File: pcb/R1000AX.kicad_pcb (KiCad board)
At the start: 4 copper layers, 175 x 65.5 mm, 140 parts, among them J1 PCIESOCKET-X1, J10 PCIESOCKET-X1, J11 PCIESOCKET-X1, J12 PCIESOCKET-X1, J13 PCIESOCKET-X1, J14 PCIESOCKET-X1, J15 PCIESOCKET-X1, J16 CONN127P-02X05, J17 USB_B_RECEPTACLE, J18 SOCKET254P-01X02, J19 COMPUTE_MOD_1, J2 PCIESOCKET-X1, J20 USB_A_RECEPTACLE_2, J25 SOCKET420P-02X04-CPU, J3 PCIESOCKET-X1, J31 USB_A_RECEPTACLE_2, J4 PCIESOCKET-X1, J5 PCIESOCKET-X1, J6 PCIESOCKET-X1, J7 PCIESOCKET-X1, J8 PCIESOCKET-X1, J81 SOCKET254P-01X02, J82 SOCKET254P-01X02, J83 SOCKET254P-01X02, J9 PCIESOCKET-X1, Q1 DMG2305UX-7, Q2 PSMN1R2-30YLC, Q3 Q_PNP_BEC, Q4 Q_NPN_BEC, Q5 Q_PNP_BEC, Q6 Q_PNP_BEC, U1 LPC1769FBD100,551, U2 AP3418, U20 M24C08-FDW6TP, U3 BD9E302EFJ-E2, U4 INA3221AIRGVR, U5 LM5060MM/NOPB, Y1 XTAL4_12MHz

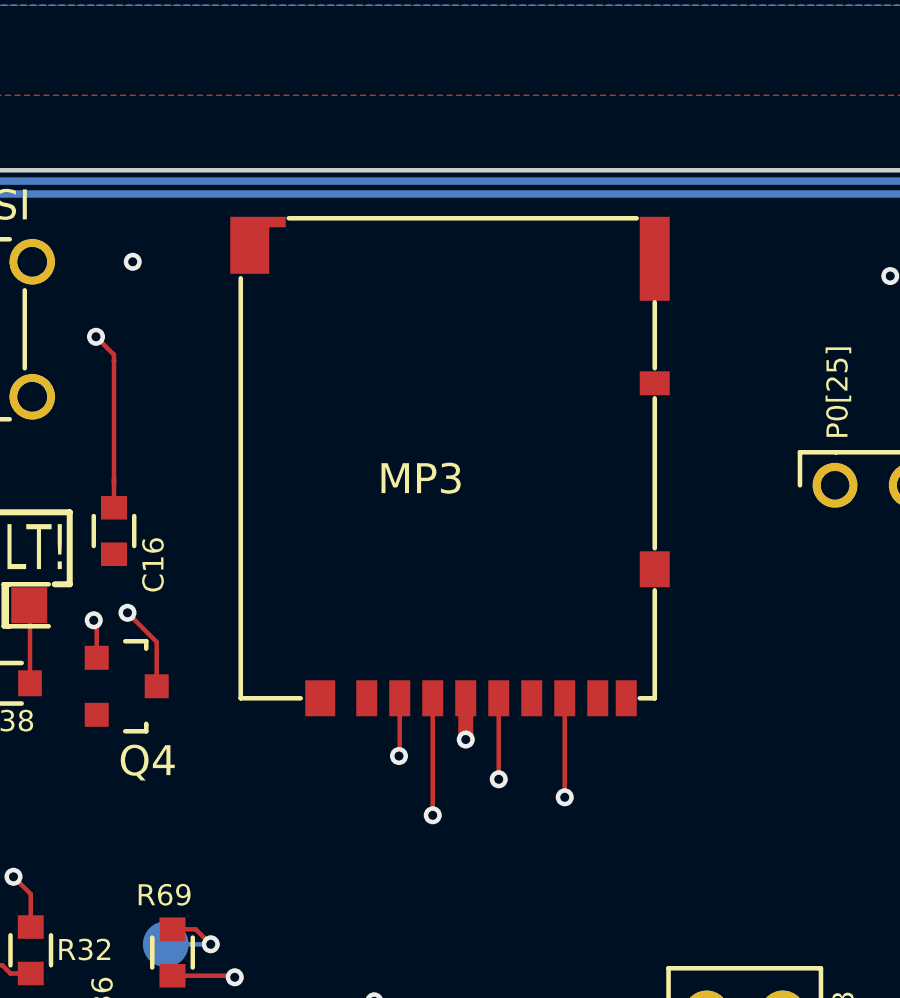
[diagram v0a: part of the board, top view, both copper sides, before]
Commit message: moved SD card more towards edge, making it accessible from case
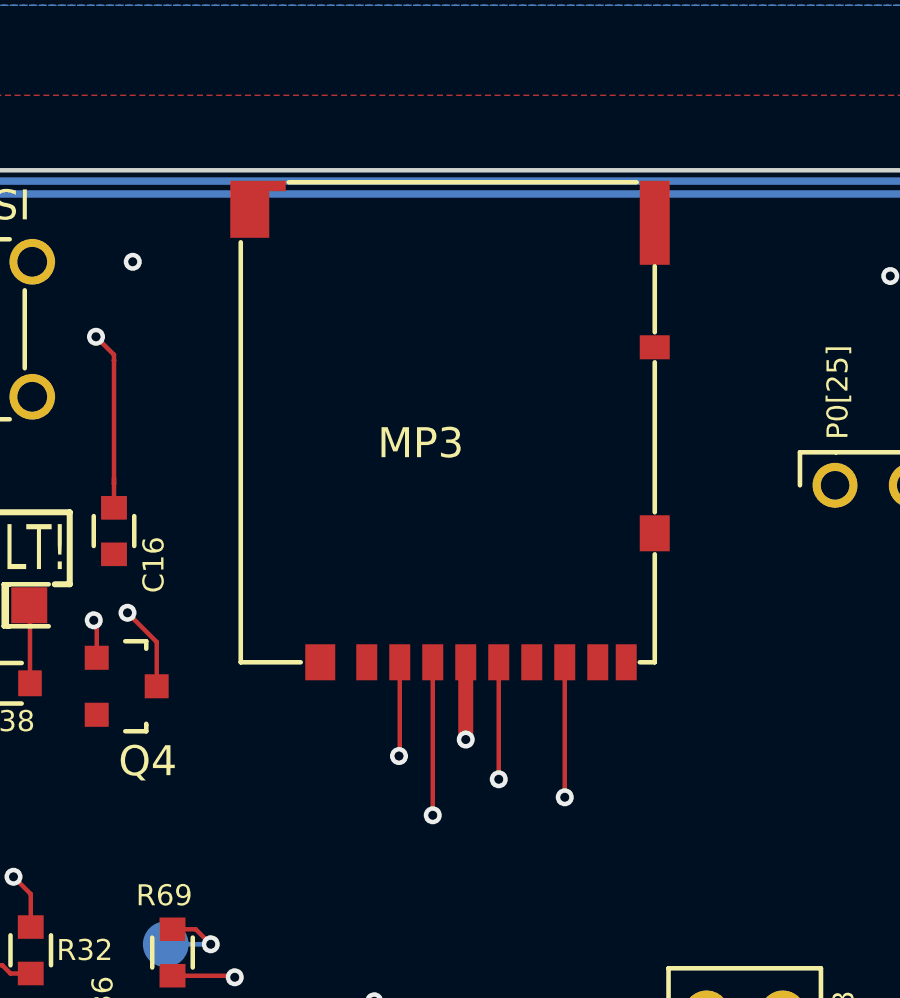
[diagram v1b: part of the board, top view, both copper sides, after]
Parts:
- moved MP3 1.20 mm to (165.8, 89.3)
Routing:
- net +3V3: track 53.4 -> 54.6 mm
- net SD_SSEL: track 52.2 -> 53.4 mm
- net SD_SCK: track 55.0 -> 56.2 mm
- net SD_MOSI: track 52.3 -> 53.5 mm
- net SD_MISO: track 56.8 -> 58.0 mm
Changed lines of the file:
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@@
     (thickness 1.6)
     (drawings 72)
-    (tracks 3447)
+    (tracks 3448)
     (zones 0)
     (modules 140)
@@
   (page A4)
   (layers
-    (0 F.Cu signal hide)
+    (0 F.Cu signal)
     (1 In1.Cu signal hide)
     (2 In2.Cu signal hide)
@@
     (pad_to_mask_clearance 0)
     (aux_axis_origin -41.6 -108.1)
-    (visible_elements 7FFEFFFF)
+    (visible_elements 7FFE7FFF)
     (pcbplotparams
       (layerselection 0x010fe_80000007)
@@
   )
   (module Main:MICROSD_RECEPTACLE_2 (layer F.Cu)
-    (at 165.8 90.5 180)
+    (at 165.8 89.3 180)
     (fp_text reference MP3 (at -1.8 6.7 180) (layer F.SilkS)
       (effects (font (size 1 1) (thickness 0.15)))
@@
   (gr_arc (start 53 137) (end 53 139) (angle 90) (layer Edge.Cuts) (width 0.15))
   (gr_line (start 51 75.5) (end 51 137) (angle 90) (layer Edge.Cuts) (width 0.15))
+  (segment (start 169.1 92.475) (end 169.1 89.9) (width 0.5) (layer F.Cu) (net 1))
+  (via (at 169.1 92.475) (size 0.6) (drill 0.3) (layers F.Cu B.Cu) (net 1))
   (segment (start 77.40076 77.55) (end 76.05 77.55) (width 0.2) (layer F.Cu) (net 1))
   (via (at 75.8 77.3) (size 0.6) (drill 0.3) (layers F.Cu B.Cu) (net 1))
   (segment (start 76.05 77.55) (end 75.8 77.3) (width 0.2) (layer F.Cu) (net 1))
-  (segment (start 169.1 91.1) (end 169.1 92.475) (width 0.5) (layer F.Cu) (net 1))
-  (via (at 169.1 92.475) (size 0.6) (drill 0.3) (layers F.Cu B.Cu) (net 1))
   (segment (start 131.7 81.2995) (end 132.6495 81.2995) (width 0.25) (layer F.Cu) (net 1))
   (via (at 132.825 81.475) (size 0.6) (drill 0.3) (layers F.Cu B.Cu) (net 1))
@@
   (segment (start 69.14 83.575) (end 66.575 83.575) (width 0.75) (layer F.Cu) (net 90))
   (segment (start 66.575 83.575) (end 66 83) (width 0.75) (layer F.Cu) (net 90))
+  (segment (start 166.9 93) (end 166.9 89.9) (width 0.15) (layer F.Cu) (net 91))
   (segment (start 161.925 93.524994) (end 166.375006 93.524994) (width 0.15) (layer In2.Cu) (net 91))
-  (segment (start 166.9 93) (end 166.9 91.1) (width 0.15) (layer F.Cu) (net 91))
   (segment (start 166.875 93.025) (end 166.9 93) (width 0.15) (layer F.Cu) (net 91))
+  (segment (start 166.9 93) (end 166.9 93) (width 0.15) (layer F.Cu) (net 91))
   (via (at 166.875 93.025) (size 0.6) (drill 0.3) (layers F.Cu B.Cu) (net 91))
   (segment (start 166.375006 93.524994) (end 166.875 93.025) (width 0.15) (layer In2.Cu) (net 91))
@@
   (segment (start 161.925736 93.524994) (end 161.925 93.524994) (width 0.15) (layer In2.Cu) (net 91))
   (segment (start 161.925 93.524994) (end 150.672792 93.524994) (width 0.15) (layer In2.Cu) (net 91))
-  (segment (start 168 95) (end 168 94.7) (width 0.15) (layer In2.Cu) (net 92))
-  (via (at 168 95) (size 0.6) (drill 0.3) (layers F.Cu B.Cu) (net 92))
-  (segment (start 168 91.1) (end 168 95) (width 0.15) (layer F.Cu) (net 92))
-  (segment (start 168 94.7) (end 167.725 94.425) (width 0.15) (layer In2.Cu) (net 92))
-  (segment (start 167.725 94.425) (end 150.3 94.425) (width 0.15) (layer In2.Cu) (net 92))
-  (segment (start 126.710281 86.775) (end 124.687363 88.797918) (width 0.15) (layer F.Cu) (net 92))
-  (segment (start 126.9 86.775) (end 126.710281 86.775) (width 0.15) (layer F.Cu) (net 92))
-  (via (at 126.9 86.775) (size 0.6) (drill 0.3) (layers F.Cu B.Cu) (net 92))
-  (segment (start 126.633463 87.041537) (end 126.9 86.775) (width 0.15) (layer In2.Cu) (net 92))
-  (segment (start 126.633463 87.316537) (end 126.633463 87.041537) (width 0.15) (layer In2.Cu) (net 92))
-  (segment (start 133.066926 93.75) (end 126.633463 87.316537) (width 0.15) (layer In2.Cu) (net 92))
-  (segment (start 149.625 93.75) (end 133.066926 93.75) (width 0.15) (layer In2.Cu) (net 92))
+  (segment (start 168 89.9) (end 168 95) (width 0.15) (layer F.Cu) (net 92))
   (segment (start 150.3 94.425) (end 149.625 93.75) (width 0.15) (layer In2.Cu) (net 92))
-  (segment (start 162 93.824996) (end 170.175004 93.824996) (width 0.15) (layer In2.Cu) (net 93))
-  (via (at 170.2 93.8) (size 0.6) (drill 0.3) (layers F.Cu B.Cu) (net 93))
-  (segment (start 170.2 93.8) (end 170.2 91.1) (width 0.15) (layer F.Cu) (net 93))
+  (segment (start 149.625 93.75) (end 133.066926 93.75) (width 0.15) (layer In2.Cu) (net 92))
+  (segment (start 133.066926 93.75) (end 126.633463 87.316537) (width 0.15) (layer In2.Cu) (net 92))
+  (segment (start 126.633463 87.316537) (end 126.633463 87.041537) (width 0.15) (layer In2.Cu) (net 92))
+  (segment (start 126.633463 87.041537) (end 126.9 86.775) (width 0.15) (layer In2.Cu) (net 92))
+  (via (at 126.9 86.775) (size 0.6) (drill 0.3) (layers F.Cu B.Cu) (net 92))
+  (segment (start 126.9 86.775) (end 126.710281 86.775) (width 0.15) (layer F.Cu) (net 92))
+  (segment (start 126.710281 86.775) (end 124.687363 88.797918) (width 0.15) (layer F.Cu) (net 92))
+  (segment (start 167.725 94.425) (end 150.3 94.425) (width 0.15) (layer In2.Cu) (net 92))
+  (segment (start 168 94.7) (end 167.725 94.425) (width 0.15) (layer In2.Cu) (net 92))
+  (via (at 168 95) (size 0.6) (drill 0.3) (layers F.Cu B.Cu) (net 92))
+  (segment (start 168 95) (end 168 94.7) (width 0.15) (layer In2.Cu) (net 92))
+  (segment (start 170.2 89.9) (end 170.2 93.8) (width 0.15) (layer F.Cu) (net 93))
   (segment (start 170.175004 93.824996) (end 170.2 93.8) (width 0.15) (layer In2.Cu) (net 93))
+  (via (at 170.2 93.8) (size 0.6) (drill 0.3) (layers F.Cu B.Cu) (net 93))
+  (segment (start 170.175004 93.824996) (end 162 93.824996) (width 0.15) (layer In2.Cu) (net 93))
   (segment (start 127.05 85) (end 123.980256 88.069744) (width 0.15) (layer F.Cu) (net 93))
   (via (at 127.05 85) (size 0.6) (drill 0.3) (layers F.Cu B.Cu) (net 93))
@@
   (segment (start 162 93.824996) (end 150.548528 93.824996) (width 0.15) (layer In2.Cu) (net 93))
   (segment (start 123.980256 88.069744) (end 123.980256 88.090812) (width 0.15) (layer F.Cu) (net 93))
-  (segment (start 163.175 94.124998) (end 169.424998 94.124998) (width 0.15) (layer In2.Cu) (net 94))
-  (via (at 172.4 94.4) (size 0.6) (drill 0.3) (layers F.Cu B.Cu) (net 94))
-  (segment (start 172.4 94.4) (end 172.4 91.1) (width 0.15) (layer F.Cu) (net 94))
-  (segment (start 169.7 94.4) (end 172.4 94.4) (width 0.15) (layer In2.Cu) (net 94))
+  (segment (start 172.4 89.9) (end 172.4 94.4) (width 0.15) (layer F.Cu) (net 94))
   (segment (start 169.424998 94.124998) (end 169.7 94.4) (width 0.15) (layer In2.Cu) (net 94))
+  (segment (start 169.7 94.4) (end 172.4 94.4) (width 0.15) (layer In2.Cu) (net 94))
+  (via (at 172.4 94.4) (size 0.6) (drill 0.3) (layers F.Cu B.Cu) (net 94))
+  (segment (start 169.424998 94.124998) (end 163.175 94.124998) (width 0.15) (layer In2.Cu) (net 94))
   (segment (start 126.878175 85.9) (end 124.33381 88.444365) (width 0.15) (layer F.Cu) (net 94))
   (segment (start 127.075 85.9) (end 126.878175 85.9) (width 0.15) (layer F.Cu) (net 94))

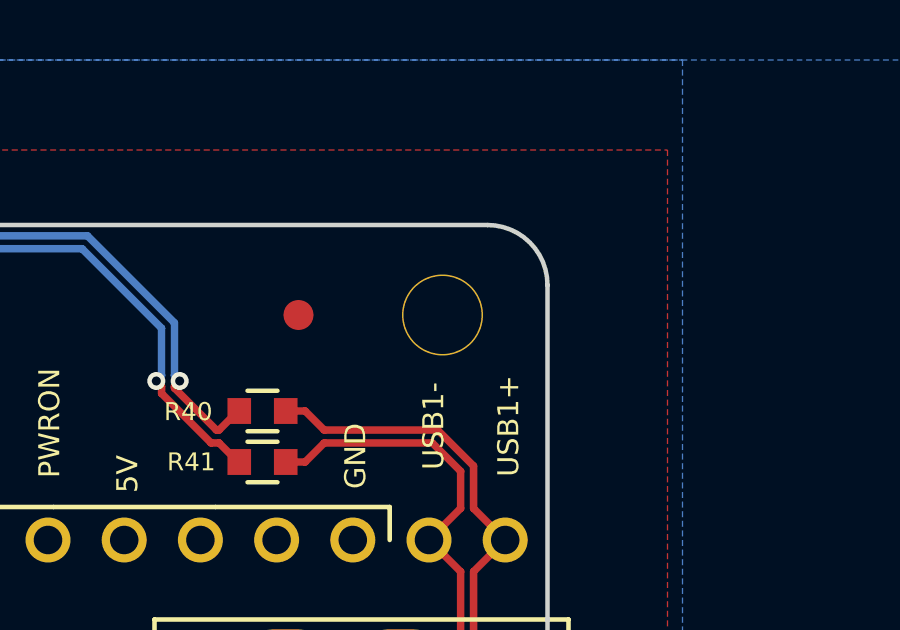
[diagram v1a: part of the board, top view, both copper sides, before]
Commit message: re-exported gerbers, moved SD card towards edge
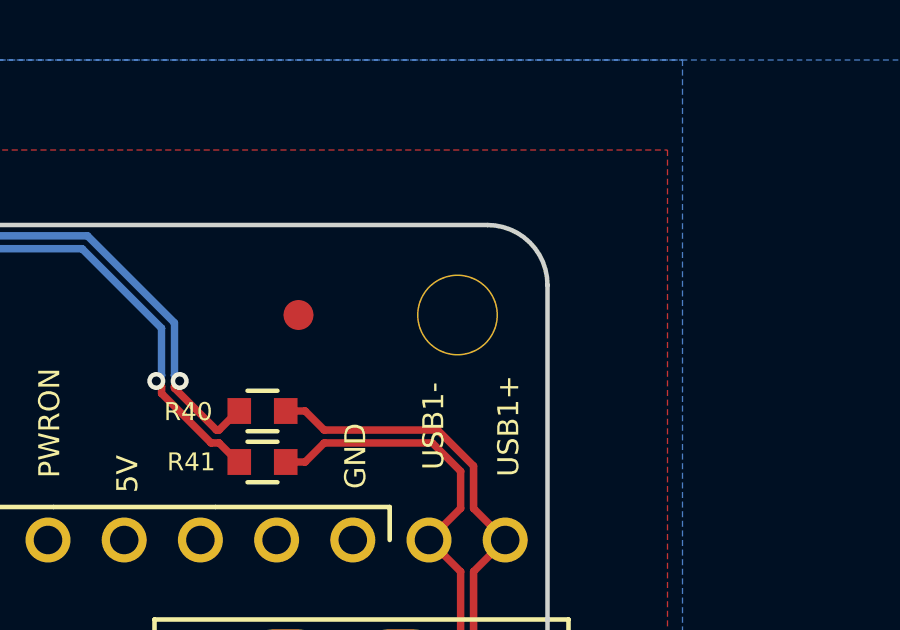
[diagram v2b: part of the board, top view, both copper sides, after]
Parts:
- moved MP8 9.38 mm to (223.0, 76.5)
- moved MP7 6.40 mm to (54.0, 136.0)
- moved MP4 1.41 mm to (223.0, 136.0)
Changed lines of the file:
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@@
     )
-  )
-  (module Main:MECH_NPTH_M3 (layer F.Cu)
-    (at 222 135)
-    (fp_text reference MP4 (at 0 -1.6) (layer F.SilkS) hide
-      (effects (font (size 1 1) (thickness 0.15)))
-    )
-    (fp_text value MECH_NPTH_M3 (at 0 -2.8) (layer F.Fab) hide
-      (effects (font (size 1 1) (thickness 0.15)))
-    )
-    (pad "" np_thru_hole circle (at 1 1) (size 2.7 2.7) (drill 2.6) (layers *.Cu *.Mask F.SilkS))
-  )
-  (module Main:MECH_NPTH_M3 (layer F.Cu)
-    (at 85 76.5)
-    (fp_text reference MP6 (at 0 -1.6) (layer F.SilkS) hide
-      (effects (font (size 1 1) (thickness 0.15)))
-    )
-    (fp_text value MECH_NPTH_M3 (at 0 -2.8) (layer F.Fab) hide
-      (effects (font (size 1 1) (thickness 0.15)))
-    )
-    (pad "" np_thru_hole circle (at 0 0) (size 2.7 2.7) (drill 2.6) (layers *.Cu *.Mask F.SilkS))
-  )
-  (module Main:MECH_NPTH_M3 (layer F.Cu)
-    (at 49 140)
-    (fp_text reference MP7 (at 0 -1.6) (layer F.SilkS) hide
-      (effects (font (size 1 1) (thickness 0.15)))
-    )
-    (fp_text value MECH_NPTH_M3 (at 0 -2.8) (layer F.Fab) hide
-      (effects (font (size 1 1) (thickness 0.15)))
-    )
-    (pad "" np_thru_hole circle (at 5 -4) (size 2.7 2.7) (drill 2.6) (layers *.Cu *.Mask F.SilkS))
-  )
-  (module Main:MECH_NPTH_M3 (layer F.Cu)
-    (at 221.8 85.8)
-    (fp_text reference MP8 (at 0 -1.6) (layer F.SilkS) hide
-      (effects (font (size 1 1) (thickness 0.15)))
-    )
-    (fp_text value MECH_NPTH_M3 (at 0 -2.8) (layer F.Fab) hide
-      (effects (font (size 1 1) (thickness 0.15)))
-    )
-    (pad "" np_thru_hole circle (at 0.7 -9.3) (size 2.7 2.7) (drill 2.6) (layers *.Cu *.Mask F.SilkS))
   )
   (module Main:COMPUTE_MOD_1 (layer F.Cu)
@@
     )
   )
+  (module Main:MECH_NPTH_M3 (layer F.Cu)
+    (at 223 136)
+    (fp_text reference MP4 (at 0 -1.6) (layer F.SilkS) hide
+      (effects (font (size 1 1) (thickness 0.15)))
+    )
+    (fp_text value MECH_NPTH_M3 (at 0 -2.8) (layer F.Fab) hide
+      (effects (font (size 1 1) (thickness 0.15)))
+    )
+    (pad "" np_thru_hole circle (at 0 0) (size 2.7 2.7) (drill 2.6) (layers *.Cu *.Mask F.SilkS))
+  )
+  (module Main:MECH_NPTH_M3 (layer F.Cu)
+    (at 54 136)
+    (fp_text reference MP7 (at 0 -1.6) (layer F.SilkS) hide
+      (effects (font (size 1 1) (thickness 0.15)))
+    )
+    (fp_text value MECH_NPTH_M3 (at 0 -2.8) (layer F.Fab) hide
+      (effects (font (size 1 1) (thickness 0.15)))
+    )
+    (pad "" np_thru_hole circle (at 0 0) (size 2.7 2.7) (drill 2.6) (layers *.Cu *.Mask F.SilkS))
+  )
+  (module Main:MECH_NPTH_M3 (layer F.Cu)
+    (at 85 76.5)
+    (fp_text reference MP6 (at 0 -1.6) (layer F.SilkS) hide
+      (effects (font (size 1 1) (thickness 0.15)))
+    )
+    (fp_text value MECH_NPTH_M3 (at 0 -2.8) (layer F.Fab) hide
+      (effects (font (size 1 1) (thickness 0.15)))
+    )
+    (pad "" np_thru_hole circle (at 0 0) (size 2.7 2.7) (drill 2.6) (layers *.Cu *.Mask F.SilkS))
+  )
+  (module Main:MECH_NPTH_M3 (layer F.Cu)
+    (at 223 76.5)
+    (fp_text reference MP8 (at 0 -1.6) (layer F.SilkS) hide
+      (effects (font (size 1 1) (thickness 0.15)))
+    )
+    (fp_text value MECH_NPTH_M3 (at 0 -2.8) (layer F.Fab) hide
+      (effects (font (size 1 1) (thickness 0.15)))
+    )
+    (pad "" np_thru_hole circle (at 0 0) (size 2.7 2.7) (drill 2.6) (layers *.Cu *.Mask F.SilkS))
+  )
   (gr_text COMPUTE (at 224.8 103.7 90) (layer F.SilkS)

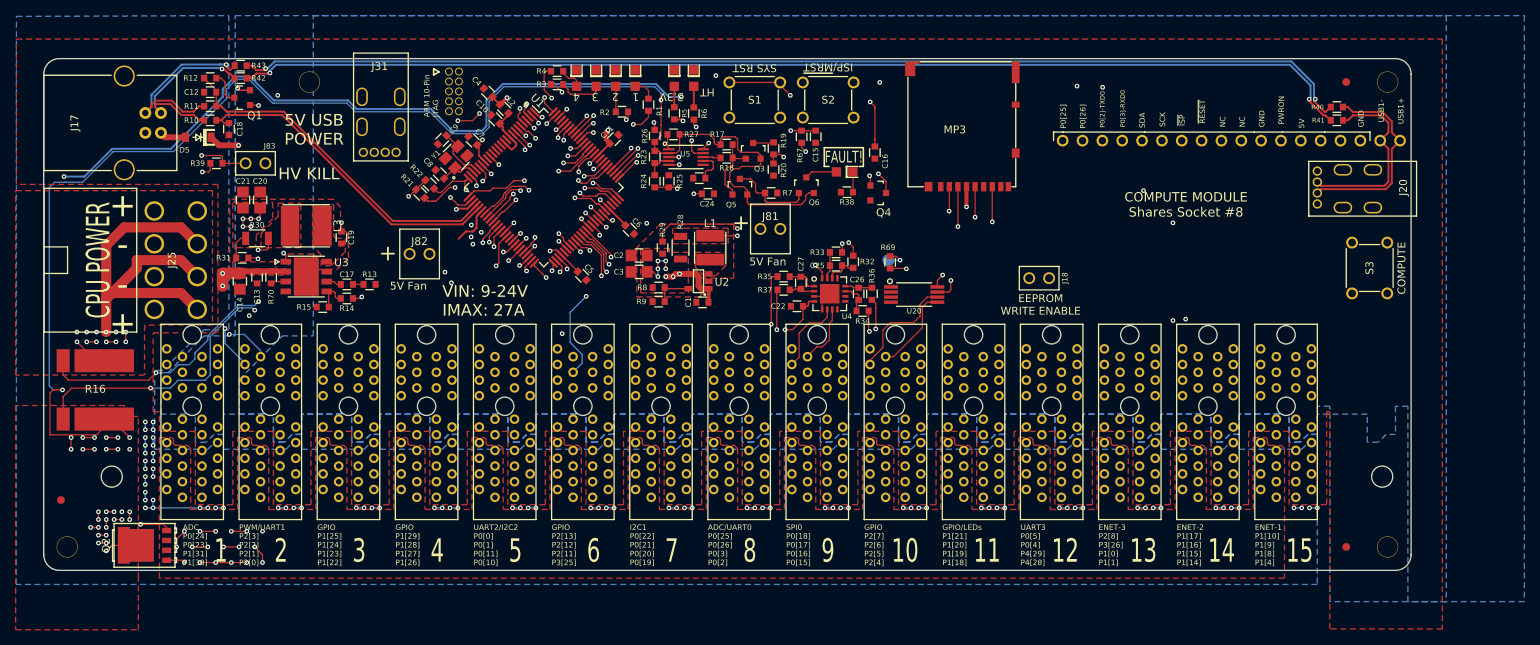
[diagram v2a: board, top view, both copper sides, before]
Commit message: fixed dimensions for tactile switches
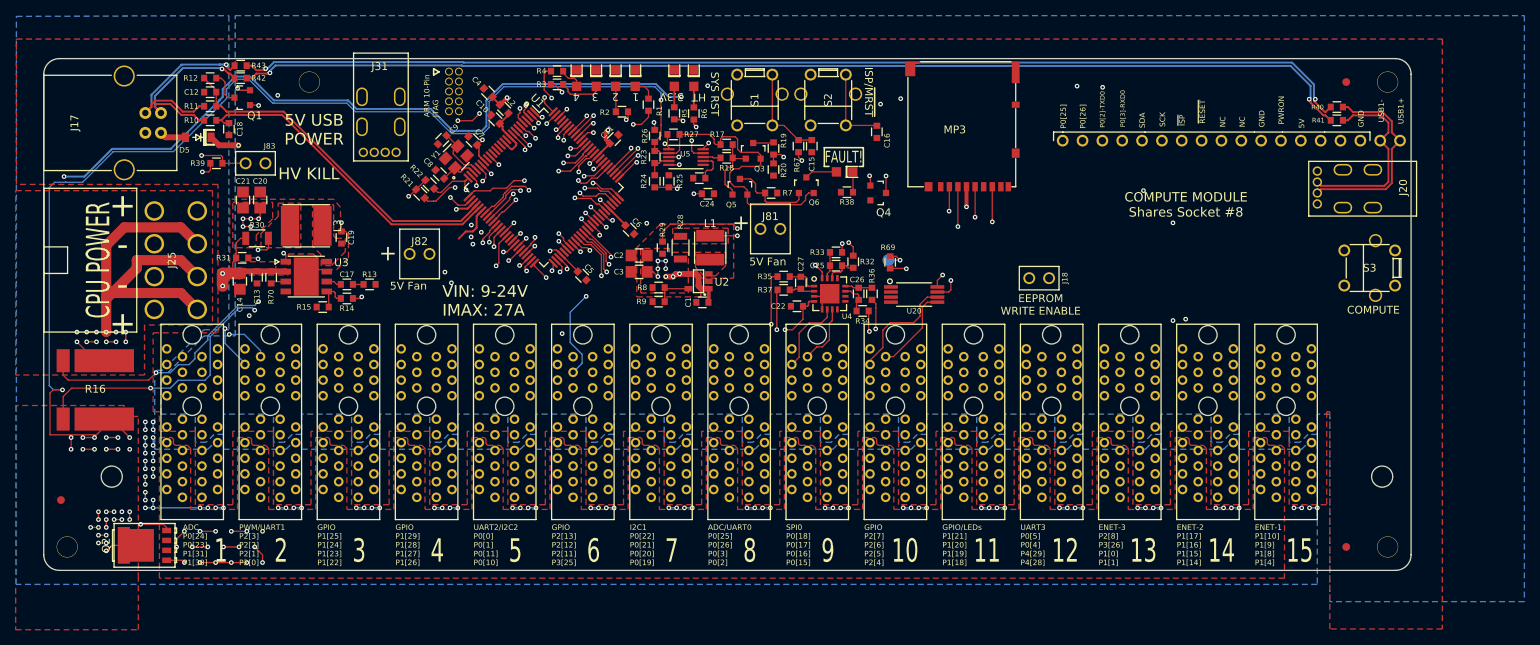
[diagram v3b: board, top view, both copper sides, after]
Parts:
- moved C16 2.66 mm to (157.6, 82.9)
- moved C15 1.30 mm to (149.3, 84.7)
- moved R67 1.26 mm to (147.6, 84.7)
- turned S1 to 270 degrees
- turned S2 to 270 degrees
- turned S3 to 180 degrees
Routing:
- net /PWRON: track 36.0 -> 29.7 mm
- net ~MRESET: track 324.7 -> 329.7 mm
- net J08.PX1.A12.P0[25]: track 150.4 -> 154.9 mm
- net J08.PX2.A13.P0[26]: track 153.5 -> 158.0 mm
- net HV_~PGD: track 139.3 -> 135.4 mm
- net /~RESET: track 130.3 -> 126.7 mm, vias 3 -> 1
- net J08.PX4.A15.P0[2]: track 140.1 -> 143.7 mm
- net J08.PX3.A14.P0[3]: track 142.0 -> 145.6 mm
- net /PowerMonitor/LM5060_GATE: track 196.8 -> 194.2 mm
- net HV_EN: track 92.5 -> 90.1 mm
- net PFET_D: track 229.8 -> 229.2 mm
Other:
- board text added: "JuicyBoard - R1000AX v1.3.2 Designed by plugg.ee Labs LLC San Jose CA, USA http://plugg.ee"
- board text removed: "JuicyBoard - R1000AX v1.3.1 Designed by plugg.ee Labs LLC San Jose CA, USA http://plugg.ee"
